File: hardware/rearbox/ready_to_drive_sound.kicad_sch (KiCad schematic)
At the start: 5 parts, among them Q5 BUK6D210

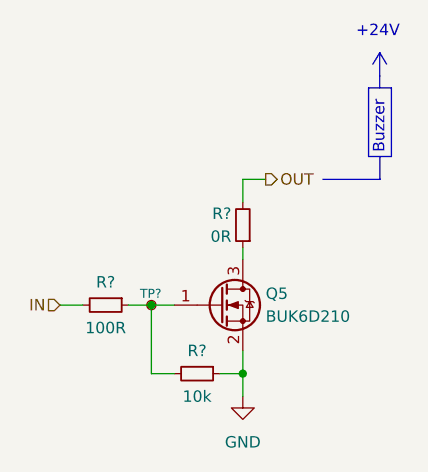
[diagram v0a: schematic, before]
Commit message: Place components on the PCB
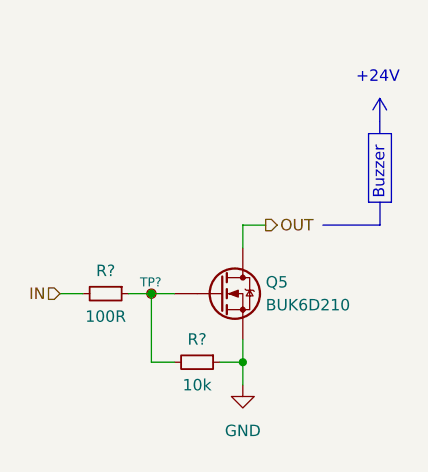
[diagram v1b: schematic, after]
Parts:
- removed R?: 0R, Resistor_SMD:R_0603_1608Metric, symbol Device:R_Small
- Q5: symbol Device:Q_NMOS_GSD -> BUK6D210:BUK6D210
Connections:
- net GND: now also Q5.4 (S), Q5.8 (S); no longer Q5.2 (S)
- net OUT: now also Q5.1 (D), Q5.2 (D), Q5.5 (D), Q5.6 (D), Q5.7 (D)
- net at R?.1, R?.2, TP?.1: now also Q5.3 (G); no longer Q5.1 (G)
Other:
- moved on the sheet: R?, TP?

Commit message: Route PCB tracks
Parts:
- Q5: footprint Package_DFN_QFN:Diodes_UDFN2020-6_Type-F -> Local_Library:Diodes_UDFN2020-6_Type-F
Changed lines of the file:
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@@
       (effects (font (size 1.27 1.27)) (justify left))
     )
-    (property "Footprint" "Package_DFN_QFN:Diodes_UDFN2020-6_Type-F" (at 147.32 120.65 0)
+    (property "Footprint" "Local_Library:Diodes_UDFN2020-6_Type-F" (at 147.32 120.65 0)
       (effects (font (size 1.27 1.27)) hide)
     )

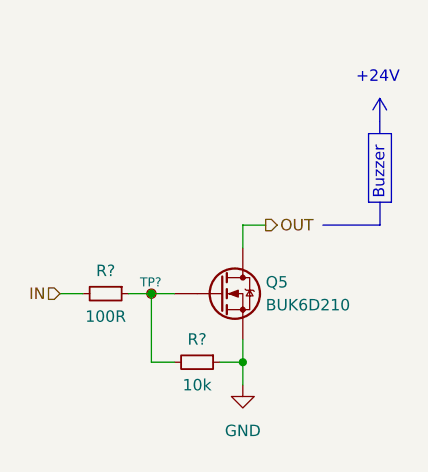
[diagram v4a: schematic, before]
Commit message: Route the tracks on the connector PCB
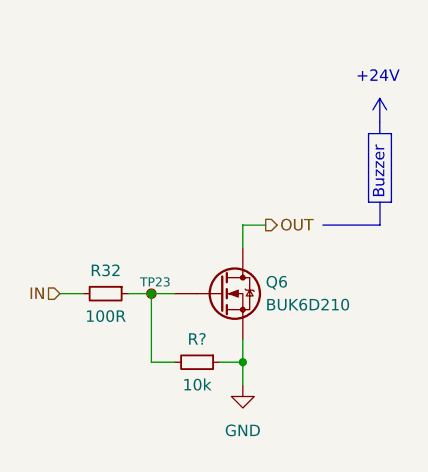
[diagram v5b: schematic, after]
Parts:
- gave numbers to parts that had none: 2
- renumbered Q5 to Q6
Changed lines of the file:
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@@
       )
       (project "rearbox"
-        (path "/b652b05a-4e3d-4ad1-b032-18886abe7d45/23ffbfb4-d932-48bb-a16b-e7ed705895f1"
-          (reference "R37") (unit 1)
-        )
-        (path "/b652b05a-4e3d-4ad1-b032-18886abe7d45/91248db3-ac16-4fb7-9cfe-25145bb94249"
-          (reference "R22") (unit 1)
-        )
-        (path "/b652b05a-4e3d-4ad1-b032-18886abe7d45/2f82735d-d185-44cc-bb86-fc399780134d"
-          (reference "R29") (unit 1)
-        )
         (path "/b652b05a-4e3d-4ad1-b032-18886abe7d45/562e38ba-d94a-4627-8fa0-e9eb7b5e4e9a"
           (reference "R33") (unit 1)
@@
   (symbol (lib_id "BUK6D210:BUK6D210") (at 146.05 107.95 0) (unit 1)
     (in_bom yes) (on_board yes) (dnp no)
-    (property "Reference" "Q5" (at 151.13 106.68 0)
+    (property "Reference" "Q6" (at 151.13 106.68 0)
       (effects (font (size 1.27 1.27)) (justify left))
     )
@@
     (instances
       (project "rearbox"
-        (path "/b652b05a-4e3d-4ad1-b032-18886abe7d45/91248db3-ac16-4fb7-9cfe-25145bb94249"
-          (reference "Q5") (unit 1)
-        )
         (path "/b652b05a-4e3d-4ad1-b032-18886abe7d45/562e38ba-d94a-4627-8fa0-e9eb7b5e4e9a"
           (reference "Q6") (unit 1)
-        )
-        (path "/b652b05a-4e3d-4ad1-b032-18886abe7d45/12f12a63-cabc-40cf-a64b-d1bd8b3dd459"
-          (reference "Q12") (unit 1)
-        )
-        (path "/b652b05a-4e3d-4ad1-b032-18886abe7d45/2f82735d-d185-44cc-bb86-fc399780134d"
-          (reference "Q4") (unit 1)
         )
       )
@@
   (symbol (lib_id "Device:R_Small") (at 133.35 107.95 270) (unit 1)
     (in_bom yes) (on_board yes) (dnp no)
-    (property "Reference" "R?" (at 133.35 105.41 90)
+    (property "Reference" "R32" (at 133.35 105.41 90)
       (effects (font (size 1.27 1.27)))
     )
@@
     (instances
       (project "rearbox"
-        (path "/b652b05a-4e3d-4ad1-b032-18886abe7d45/91248db3-ac16-4fb7-9cfe-25145bb94249"
-          (reference "R?") (unit 1)
-        )
-        (path "/b652b05a-4e3d-4ad1-b032-18886abe7d45"
-          (reference "R?") (unit 1)
-        )
         (path "/b652b05a-4e3d-4ad1-b032-18886abe7d45/562e38ba-d94a-4627-8fa0-e9eb7b5e4e9a"
           (reference "R32") (unit 1)
-        )
-        (path "/b652b05a-4e3d-4ad1-b032-18886abe7d45/6999686b-4026-4ea7-9227-634603a79198"
-          (reference "R?") (unit 1)
-        )
-        (path "/b652b05a-4e3d-4ad1-b032-18886abe7d45/12f12a63-cabc-40cf-a64b-d1bd8b3dd459"
-          (reference "R144") (unit 1)
-        )
-        (path "/b652b05a-4e3d-4ad1-b032-18886abe7d45/2f82735d-d185-44cc-bb86-fc399780134d"
-          (reference "R28") (unit 1)
         )
       )
@@
   (symbol (lib_id "power:GND") (at 148.59 118.11 0) (unit 1)
     (in_bom yes) (on_board yes) (dnp no)
-    (property "Reference" "#PWR?" (at 148.59 124.46 0)
+    (property "Reference" "#PWR094" (at 148.59 124.46 0)
       (effects (font (size 1.27 1.27)) hide)
     )
@@
     (instances
       (project "rearbox"
-        (path "/b652b05a-4e3d-4ad1-b032-18886abe7d45/91248db3-ac16-4fb7-9cfe-25145bb94249"
-          (reference "#PWR?") (unit 1)
-        )
-        (path "/b652b05a-4e3d-4ad1-b032-18886abe7d45"
-          (reference "#PWR?") (unit 1)
-        )
         (path "/b652b05a-4e3d-4ad1-b032-18886abe7d45/562e38ba-d94a-4627-8fa0-e9eb7b5e4e9a"
           (reference "#PWR094") (unit 1)
-        )
-        (path "/b652b05a-4e3d-4ad1-b032-18886abe7d45/6999686b-4026-4ea7-9227-634603a79198"
-          (reference "#PWR?") (unit 1)
-        )
-        (path "/b652b05a-4e3d-4ad1-b032-18886abe7d45/12f12a63-cabc-40cf-a64b-d1bd8b3dd459"
-          (reference "#PWR0198") (unit 1)
-        )
-        (path "/b652b05a-4e3d-4ad1-b032-18886abe7d45/2f82735d-d185-44cc-bb86-fc399780134d"
-          (reference "#PWR069") (unit 1)
         )
       )
@@
   (symbol (lib_id "Connector:TestPoint_Small") (at 138.43 107.95 0) (unit 1)
     (in_bom yes) (on_board yes) (dnp no)
-    (property "Reference" "TP?" (at 137.16 106.68 0)
+    (property "Reference" "TP23" (at 137.16 106.68 0)
       (effects (font (size 1 1)) (justify left))
     )
@@
     (instances
       (project "rearbox"
-        (path "/b652b05a-4e3d-4ad1-b032-18886abe7d45/38408e41-dfb1-4c27-acb0-3f1224cc8789"
-          (reference "TP?") (unit 1)
-        )
-        (path "/b652b05a-4e3d-4ad1-b032-18886abe7d45/38408e41-dfb1-4c27-acb0-3f1224cc8789/eec2c93a-0fce-4d3a-ab43-9e1e0481c06c"
-          (reference "TP3") (unit 1)
-        )
-        (path "/b652b05a-4e3d-4ad1-b032-18886abe7d45/38408e41-dfb1-4c27-acb0-3f1224cc8789/f1ed15a3-9302-436f-b25a-713477aeadf3"
-          (reference "TP1") (unit 1)
-        )
         (path "/b652b05a-4e3d-4ad1-b032-18886abe7d45/562e38ba-d94a-4627-8fa0-e9eb7b5e4e9a"
           (reference "TP23") (unit 1)
         )
-        (path "/b652b05a-4e3d-4ad1-b032-18886abe7d45/12f12a63-cabc-40cf-a64b-d1bd8b3dd459"
-          (reference "TP64") (unit 1)
-        )
-        (path "/b652b05a-4e3d-4ad1-b032-18886abe7d45/2f82735d-d185-44cc-bb86-fc399780134d"
-          (reference "TP17") (unit 1)
-        )
       )

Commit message: Fix measurement bridges polarity
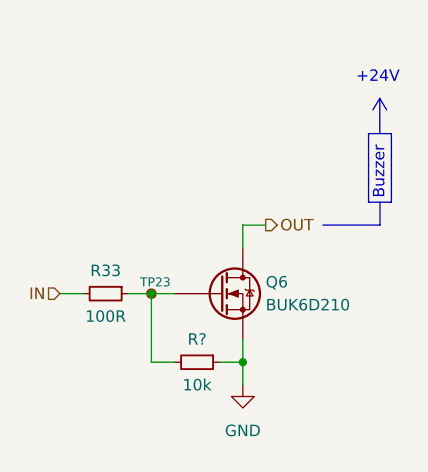
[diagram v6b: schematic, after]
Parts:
- renumbered R32 to R33
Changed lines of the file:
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@@
   (title_block
     (title "Ready to Drive Sound")
-    (date "2023-11-17")
+    (date "2024-04-28")
     (rev "${REVISION}")
     (company "Author: I. Kajdan")
@@
       (project "rearbox"
         (path "/b652b05a-4e3d-4ad1-b032-18886abe7d45/562e38ba-d94a-4627-8fa0-e9eb7b5e4e9a"
-          (reference "R33") (unit 1)
+          (reference "R34") (unit 1)
         )
       )
@@
   (symbol (lib_id "Device:R_Small") (at 133.35 107.95 270) (unit 1)
     (in_bom yes) (on_board yes) (dnp no)
-    (property "Reference" "R32" (at 133.35 105.41 90)
+    (property "Reference" "R33" (at 133.35 105.41 90)
       (effects (font (size 1.27 1.27)))
     )
@@
       (project "rearbox"
         (path "/b652b05a-4e3d-4ad1-b032-18886abe7d45/562e38ba-d94a-4627-8fa0-e9eb7b5e4e9a"
-          (reference "R32") (unit 1)
+          (reference "R33") (unit 1)
         )
       )
@@
   (symbol (lib_id "power:GND") (at 148.59 118.11 0) (unit 1)
     (in_bom yes) (on_board yes) (dnp no)
-    (property "Reference" "#PWR094" (at 148.59 124.46 0)
+    (property "Reference" "#PWR095" (at 148.59 124.46 0)
       (effects (font (size 1.27 1.27)) hide)
     )
@@
       (project "rearbox"
         (path "/b652b05a-4e3d-4ad1-b032-18886abe7d45/562e38ba-d94a-4627-8fa0-e9eb7b5e4e9a"
-          (reference "#PWR094") (unit 1)
+          (reference "#PWR095") (unit 1)
         )
       )
